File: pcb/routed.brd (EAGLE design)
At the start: 31.8 x 31.8 mm, 85 parts, among them U2 CC430F5137IRGZR, X1 CRYSTALS-NOGND-IQXC-25, X2 FA-128

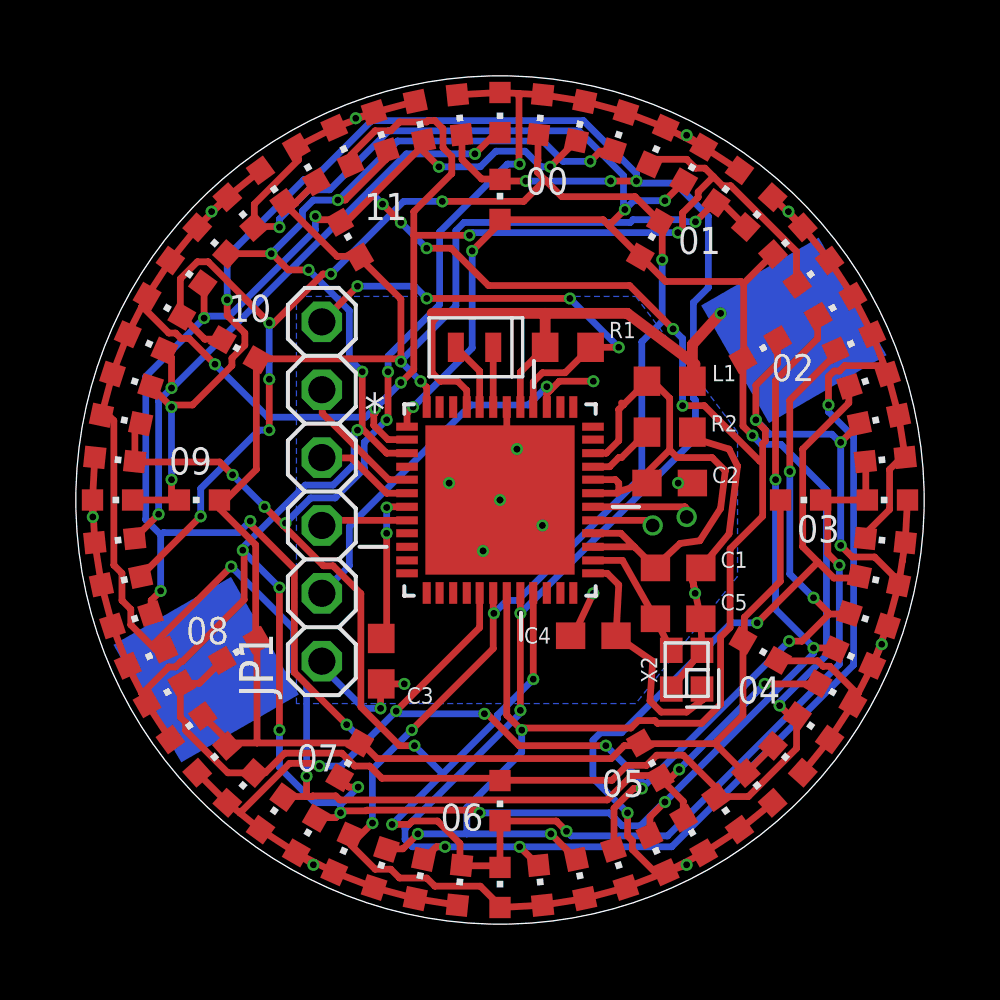
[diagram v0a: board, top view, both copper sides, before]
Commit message: move labels and 1x6 around; issues with the additional vcc line
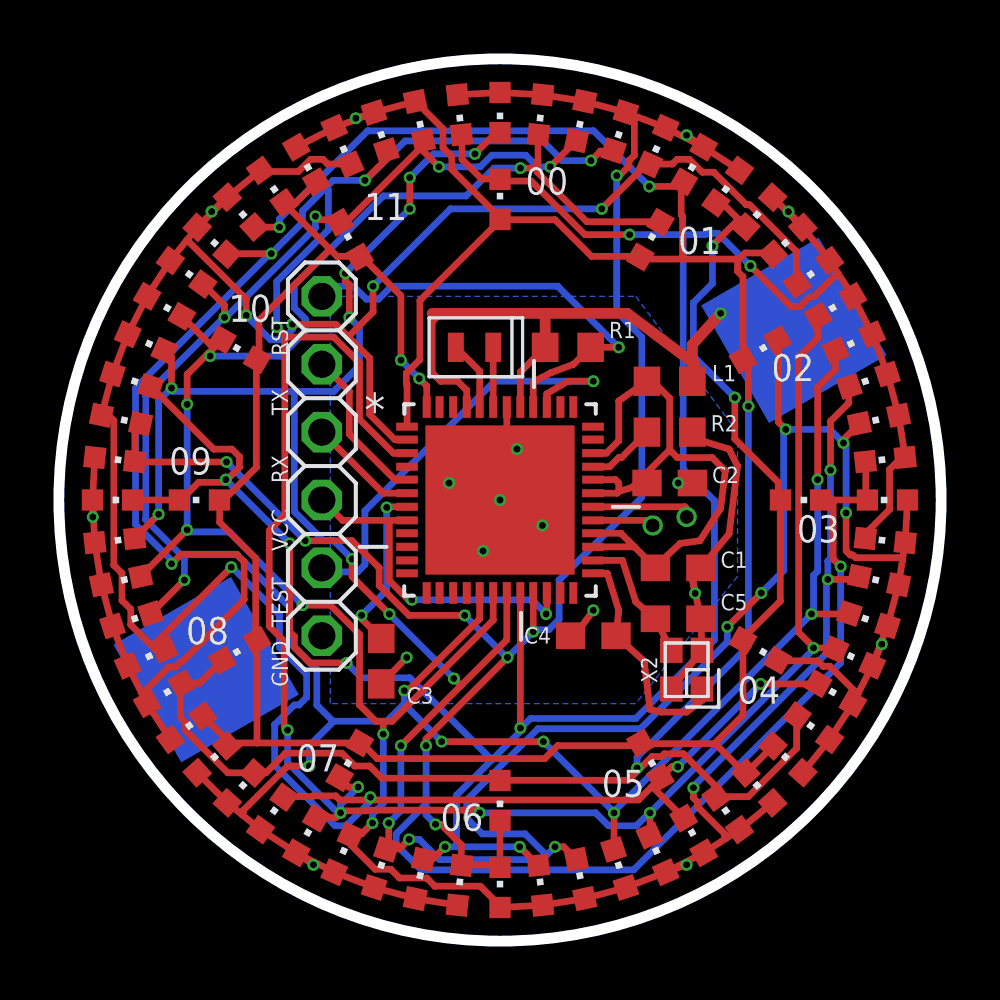
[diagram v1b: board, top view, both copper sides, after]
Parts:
- moved JP1 0.95 mm to (18.7, 26.7)
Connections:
- removed net DVCC_3: U2.22
- net BSL_VCC: now also U2.22
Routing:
- net B1: track 123.5 -> 98.9 mm, vias 12 -> 9
- net B5: track 107.7 -> 126.0 mm, vias 16 -> 12
- net B3: track 114.0 -> 99.0 mm, vias 13 -> 11
- net BSL_VCC: track 3.27 -> 12.9 mm, vias 0 -> 2
- net B6: track 110.1 -> 104.4 mm, vias 10 -> 9
- net B4: track 106.4 -> 101.4 mm, vias 16 -> 13
- net B0: track 96.2 -> 100.5 mm, vias 12 -> 10
- net B7: track 101.3 -> 105.5 mm, vias 8 -> 5
- net GND: track 34.6 -> 30.6 mm, vias 10 -> 9
- net B8: track 84.0 -> 80.3 mm, vias 3 -> 4
- net B2: track 111.7 -> 114.8 mm, vias 15 -> 20
- net BSL_TEST: track 15.1 -> 16.7 mm, vias 2 -> 1
- net BSL_TX: track 5.09 -> 5.91 mm
- net VCORE: track 5.76 -> 6.37 mm
- net BSL_RST: track 17.3 -> 17.2 mm, vias 4 -> 1
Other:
- board size 31.8 x 31.8 mm -> 33 x 33 mm
- board text added: "GND"
- board text added: "RST"
- board text added: "RX"
- board text added: "TEST"
- board text added: "TX"
- board text added: "VCC"

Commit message: replace with "1x6 lock" part
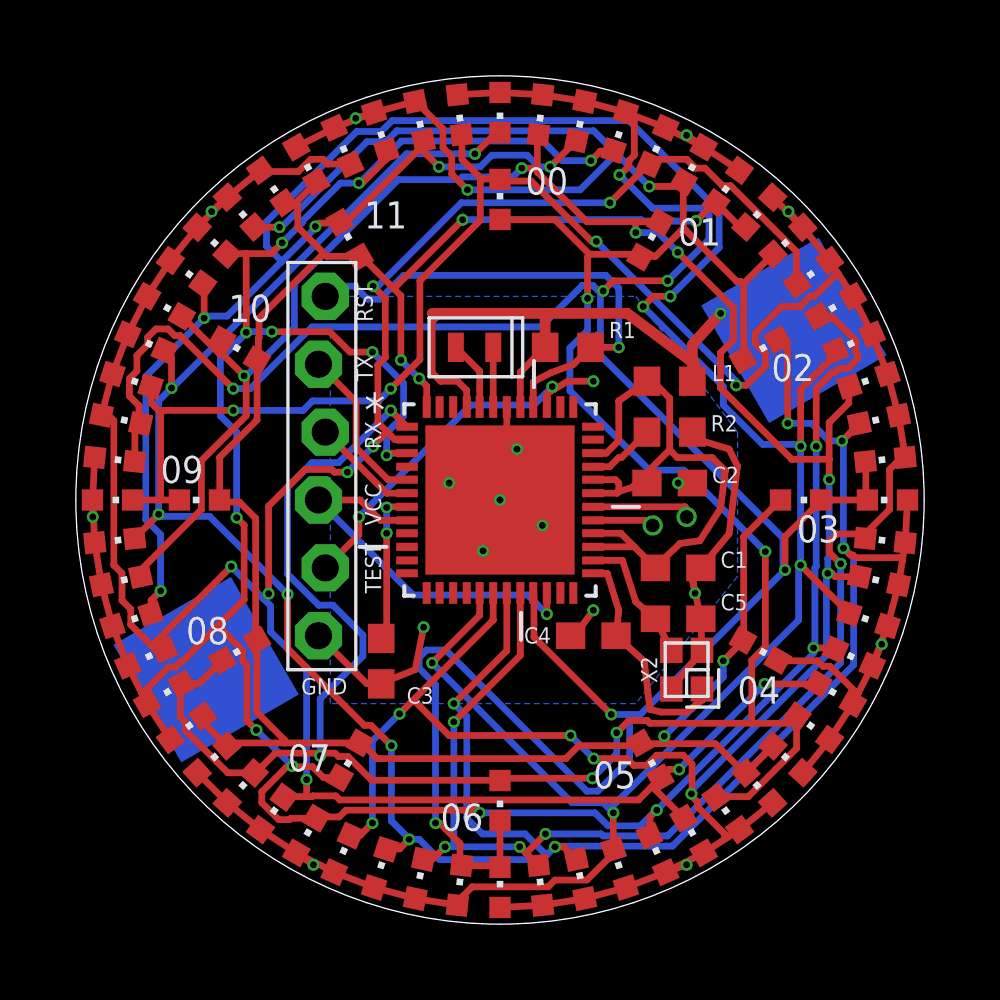
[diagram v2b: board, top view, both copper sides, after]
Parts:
- JP1: device adafruit:1X06 -> adafruit:1X06-BIGLOCK
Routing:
- net B4: track 101.4 -> 123.0 mm, vias 13 -> 12
- net B7: track 105.5 -> 126.4 mm, vias 5 -> 10
- net B5: track 126.0 -> 110.3 mm, vias 12 -> 15
- net B0: track 100.5 -> 107.7 mm, vias 10 -> 8
- net B3: track 99.0 -> 106.0 mm, vias 11 -> 12
- net B2: track 114.8 -> 109.2 mm, vias 20 -> 12
- net GND: track 30.6 -> 35.3 mm
- net B6: track 104.4 -> 100.1 mm, vias 9 -> 10
- net B8: track 80.3 -> 82.9 mm, vias 4 -> 6
- net BSL_TEST: track 16.7 -> 14.2 mm, vias 1 -> 3
- net BSL_VCC: track 12.9 -> 14.8 mm, vias 2 -> 1
- net BSL_RST: track 17.2 -> 18.7 mm
- net B1: track 98.9 -> 98.1 mm, vias 9 -> 10
- net VCORE: track 6.37 -> 5.76 mm
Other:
- board size 33 x 33 mm -> 31.8 x 31.8 mm
